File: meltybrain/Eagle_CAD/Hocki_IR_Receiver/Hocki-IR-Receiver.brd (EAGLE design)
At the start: 33 x 34 mm, 63 parts, among them U1 OPA2380AIDGKR, U10 LMH6612MAX/NOPB, U11 LMH6612MAX/NOPB, U2 OPA2380AIDGKR, U3 TLV3502AIDCNR, U4 TLV3502AIDCNR, U5 SN74LVC1G58DCKR, U6 NL27WZ32USG, U7 TMUX1204DGSR, U8 LP38693MP-5.0/NOPB, U9 TLV73310PDBVT

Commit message: added bandpass filter to control and updated ir
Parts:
- R10, R11, R3, R4: value 10k -> 500
- R17, R19: value 3.33k -> 100
- R18, R20: value 10k -> 300
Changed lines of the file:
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@@
 <drawing>
 <settings>
-<setting alwaysvectorfont="yes"/>
+<setting alwaysvectorfont="no"/>
 <setting verticaltext="up"/>
 </settings>
@@
 <attribute name="VALUE" x="5.365" y="27.095" size="1.27" layer="27"/>
 </element>
-<element name="R10" library="resistor" library_urn="urn:adsk.eagle:library:348" package="R0603" package3d_urn="urn:adsk.eagle:package:26057/1" value="10k" x="2" y="3" smashed="yes" rot="R180">
+<element name="R10" library="resistor" library_urn="urn:adsk.eagle:library:348" package="R0603" package3d_urn="urn:adsk.eagle:package:26057/1" value="500" x="2" y="3" smashed="yes" rot="R180">
 <attribute name="NAME" x="3.235" y="2.265" size="0.8128" layer="25" rot="R180"/>
 <attribute name="VALUE" x="2.635" y="4.905" size="1.27" layer="27" rot="R180"/>
 </element>
-<element name="R11" library="resistor" library_urn="urn:adsk.eagle:library:348" package="R0603" package3d_urn="urn:adsk.eagle:package:26057/1" value="10k" x="5" y="3" smashed="yes" rot="R180">
+<element name="R11" library="resistor" library_urn="urn:adsk.eagle:library:348" package="R0603" package3d_urn="urn:adsk.eagle:package:26057/1" value="500" x="5" y="3" smashed="yes" rot="R180">
 <attribute name="NAME" x="6.335" y="2.265" size="0.8128" layer="25" rot="R180"/>
 <attribute name="VALUE" x="5.635" y="4.905" size="1.27" layer="27" rot="R180"/>
@@
 <attribute name="VALUE" x="25.905" y="4.365" size="1.27" layer="27" rot="R90"/>
 </element>
-<element name="R17" library="resistor" library_urn="urn:adsk.eagle:library:348" package="R0603" package3d_urn="urn:adsk.eagle:package:26057/1" value="3.33k" x="19" y="26" smashed="yes" rot="R180">
+<element name="R17" library="resistor" library_urn="urn:adsk.eagle:library:348" package="R0603" package3d_urn="urn:adsk.eagle:package:26057/1" value="100" x="19" y="26" smashed="yes" rot="R180">
 <attribute name="NAME" x="19.635" y="25.265" size="0.8128" layer="25" rot="R180"/>
 <attribute name="VALUE" x="19.635" y="27.905" size="1.27" layer="27" rot="R180"/>
 </element>
-<element name="R18" library="resistor" library_urn="urn:adsk.eagle:library:348" package="R0603" package3d_urn="urn:adsk.eagle:package:26057/1" value="10k" x="21" y="24" smashed="yes" rot="R180">
+<element name="R18" library="resistor" library_urn="urn:adsk.eagle:library:348" package="R0603" package3d_urn="urn:adsk.eagle:package:26057/1" value="300" x="21" y="24" smashed="yes" rot="R180">
 <attribute name="NAME" x="20.765" y="24.735" size="0.8128" layer="25"/>
 <attribute name="VALUE" x="21.635" y="25.905" size="1.27" layer="27" rot="R180"/>
 </element>
-<element name="R19" library="resistor" library_urn="urn:adsk.eagle:library:348" package="R0603" package3d_urn="urn:adsk.eagle:package:26057/1" value="3.33k" x="21" y="2" smashed="yes">
+<element name="R19" library="resistor" library_urn="urn:adsk.eagle:library:348" package="R0603" package3d_urn="urn:adsk.eagle:package:26057/1" value="100" x="21" y="2" smashed="yes">
 <attribute name="NAME" x="19.665" y="2.535" size="0.8128" layer="25"/>
 <attribute name="VALUE" x="20.365" y="0.095" size="1.27" layer="27"/>
@@
 <attribute name="VALUE" x="5.365" y="18.095" size="1.27" layer="27"/>
 </element>
-<element name="R20" library="resistor" library_urn="urn:adsk.eagle:library:348" package="R0603" package3d_urn="urn:adsk.eagle:package:26057/1" value="10k" x="21" y="4" smashed="yes" rot="R180">
+<element name="R20" library="resistor" library_urn="urn:adsk.eagle:library:348" package="R0603" package3d_urn="urn:adsk.eagle:package:26057/1" value="300" x="21" y="4" smashed="yes" rot="R180">
 <attribute name="NAME" x="20.635" y="5.365" size="0.8128" layer="25" rot="R180"/>
 <attribute name="VALUE" x="21.635" y="5.905" size="1.27" layer="27" rot="R180"/>
@@
 <attribute name="VALUE" x="15.365" y="10.095" size="1.27" layer="27"/>
 </element>
-<element name="R3" library="resistor" library_urn="urn:adsk.eagle:library:348" package="R0603" package3d_urn="urn:adsk.eagle:package:26057/1" value="10k" x="2" y="32" smashed="yes" rot="R180">
+<element name="R3" library="resistor" library_urn="urn:adsk.eagle:library:348" package="R0603" package3d_urn="urn:adsk.eagle:package:26057/1" value="500" x="2" y="32" smashed="yes" rot="R180">
 <attribute name="NAME" x="2.735" y="33.565" size="0.8128" layer="25" rot="R180"/>
 <attribute name="VALUE" x="2.635" y="33.905" size="1.27" layer="27" rot="R180"/>
 </element>
-<element name="R4" library="resistor" library_urn="urn:adsk.eagle:library:348" package="R0603" package3d_urn="urn:adsk.eagle:package:26057/1" value="10k" x="5" y="32" smashed="yes" rot="R180">
+<element name="R4" library="resistor" library_urn="urn:adsk.eagle:library:348" package="R0603" package3d_urn="urn:adsk.eagle:package:26057/1" value="500" x="5" y="32" smashed="yes" rot="R180">
 <attribute name="NAME" x="5.735" y="33.565" size="0.8128" layer="25" rot="R180"/>
 <attribute name="VALUE" x="5.635" y="33.905" size="1.27" layer="27" rot="R180"/>

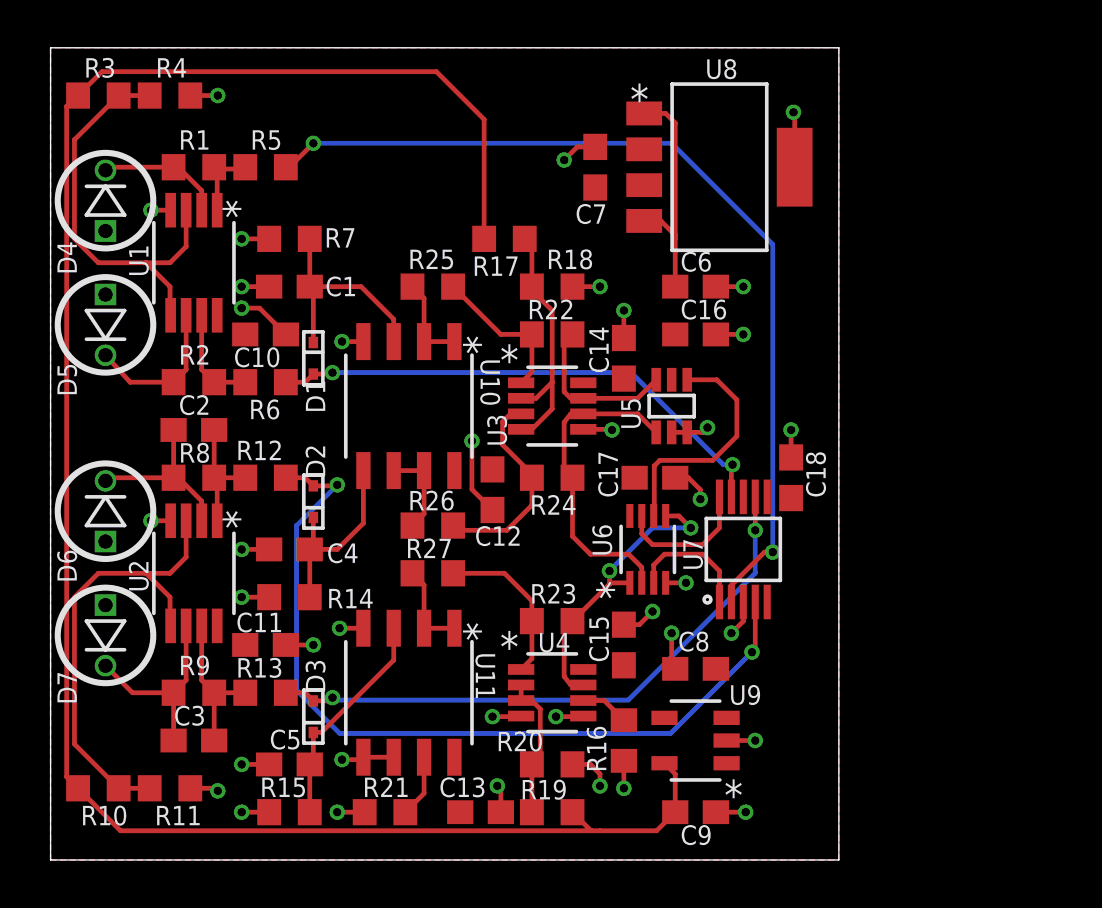
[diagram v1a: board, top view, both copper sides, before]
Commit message: Edited mutiplexers and resistors, added holes
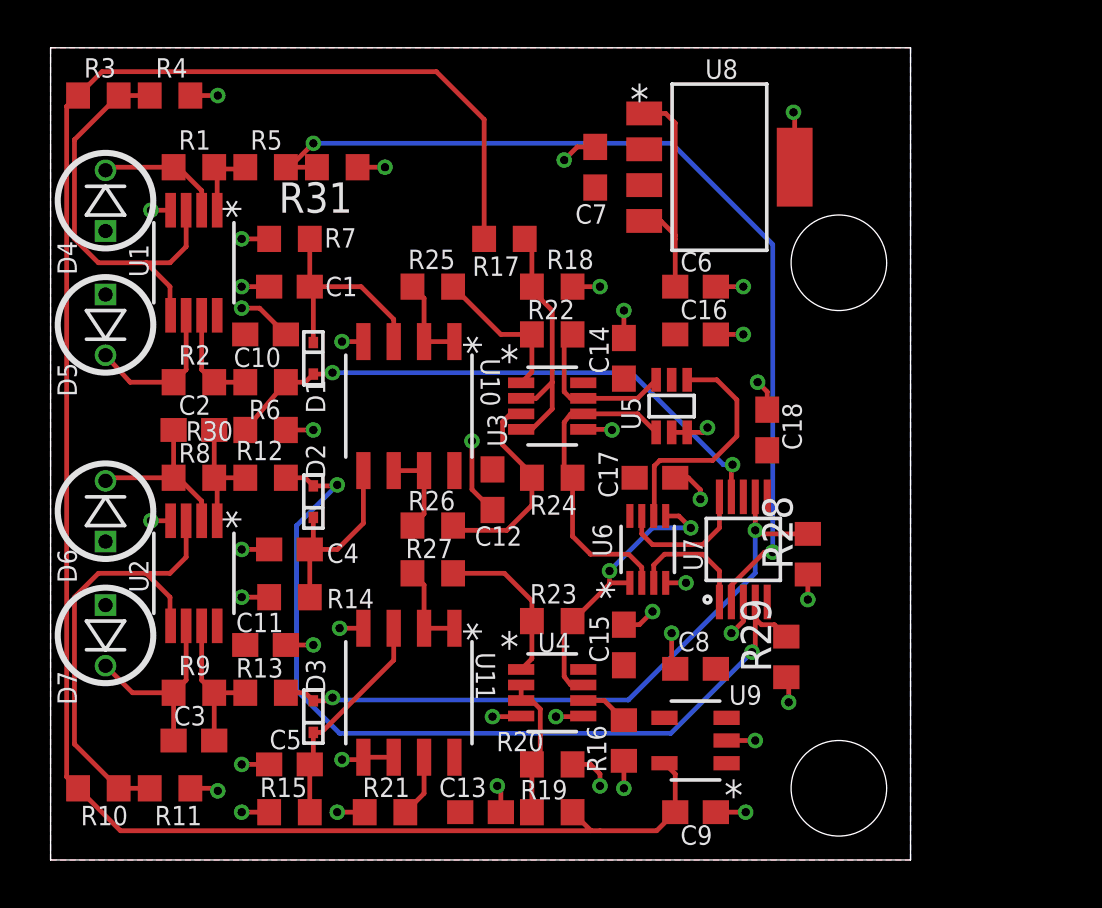
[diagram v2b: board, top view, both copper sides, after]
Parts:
- added R28, R29, R30, R31: 500, resistor:R0603
- R16, R21: value 10k -> 500
- moved C18 2.24 mm to (30.0, 18.0)
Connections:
- net 100KGAIN: now also R29.2
- net 10KGAIN: now also R28.2
- net 10MGAIN: now also R31.2
- net 1MGAIN: now also R30.2
- net GND: now also R28.1, R29.1, R30.1, R31.1
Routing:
- net GND: track 51.6 -> 55.8 mm, vias 38 -> 42
- net 1MGAIN: track 21.8 -> 24.5 mm
- net 100KGAIN: track 35.0 -> 37.3 mm
- net 10KGAIN: track 25.3 -> 27.5 mm
- net 10MGAIN: track 38.4 -> 39.6 mm
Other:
- board size 33 x 34 mm -> 36 x 34 mm
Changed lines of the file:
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@@
 <?xml version="1.0" encoding="utf-8"?>
 <!DOCTYPE eagle SYSTEM "eagle.dtd">
-<eagle version="9.5.2">
+<eagle version="9.5.1">
 <drawing>
 <settings>
@@
 <fusionsync huburn="a.cGVyc29uYWw6dWUyZDhlY2M3" projecturn="a.cGVyc29uYWw6dWUyZDhlY2M3IzIwMjAwNzEyMzE1MDc1MjU2" f3durn="urn:adsk.wipprod:dm.lineage:OuSaG_R2Q9mGFnPAEtv9Kg" pcbguid="ced57c46-fdd1-4c9d-a043-21a067a15f17" lastpulledtime="" lastsyncedchangeguid="69a52050-c321-50c1-0946-32a0d233b772"/>
 <plain>
-<wire x1="0" y1="0" x2="33" y2="0" width="0" layer="20"/>
-<wire x1="33" y1="0" x2="33" y2="34" width="0" layer="20"/>
-<wire x1="33" y1="34" x2="0" y2="34" width="0" layer="20"/>
+<wire x1="0" y1="0" x2="36" y2="0" width="0" layer="20"/>
+<wire x1="36" y1="0" x2="36" y2="34" width="0" layer="20"/>
+<wire x1="36" y1="34" x2="0" y2="34" width="0" layer="20"/>
 <wire x1="0" y1="34" x2="0" y2="0" width="0" layer="20"/>
+<hole x="33" y="3" drill="4"/>
+<hole x="33" y="25" drill="4"/>
 </plain>
 <attributes>
@@
 <attribute name="VALUE" x="9.365" y="0.095" size="1.27" layer="27"/>
 </element>
-<element name="R16" library="resistor" library_urn="urn:adsk.eagle:library:348" package="R0603" package3d_urn="urn:adsk.eagle:package:26057/1" value="10k" x="24" y="5" smashed="yes" rot="R90">
+<element name="R16" library="resistor" library_urn="urn:adsk.eagle:library:348" package="R0603" package3d_urn="urn:adsk.eagle:package:26057/1" value="500" x="24" y="5" smashed="yes" rot="R90">
 <attribute name="NAME" x="23.265" y="3.665" size="0.8128" layer="25" rot="R90"/>
 <attribute name="VALUE" x="25.905" y="4.365" size="1.27" layer="27" rot="R90"/>
@@
 <attribute name="VALUE" x="21.635" y="5.905" size="1.27" layer="27" rot="R180"/>
 </element>
-<element name="R21" library="resistor" library_urn="urn:adsk.eagle:library:348" package="R0603" package3d_urn="urn:adsk.eagle:package:26057/1" value="10k" x="14" y="2" smashed="yes">
+<element name="R21" library="resistor" library_urn="urn:adsk.eagle:library:348" package="R0603" package3d_urn="urn:adsk.eagle:package:26057/1" value="500" x="14" y="2" smashed="yes">
 <attribute name="NAME" x="13.065" y="2.635" size="0.8128" layer="25"/>
 <attribute name="VALUE" x="13.365" y="0.095" size="1.27" layer="27"/>
@@
 <attribute name="VALUE" x="24.665" y="14.095" size="1.27" layer="27"/>
 </element>
-<element name="C18" library="rcl" library_urn="urn:adsk.eagle:library:334" package="C0603" package3d_urn="urn:adsk.eagle:package:23616/2" value="0.1u" x="31" y="16" smashed="yes" rot="R90">
-<attribute name="NAME" x="31.635" y="17.135" size="0.8128" layer="25" rot="R270"/>
-<attribute name="POPULARITY" value="37" x="31" y="16" size="1.778" layer="27" rot="R90" display="off"/>
-<attribute name="SPICEPREFIX" value="C" x="31" y="16" size="1.778" layer="27" rot="R90" display="off"/>
-<attribute name="VALUE" x="32.905" y="15.365" size="1.27" layer="27" rot="R90"/>
+<element name="C18" library="rcl" library_urn="urn:adsk.eagle:library:334" package="C0603" package3d_urn="urn:adsk.eagle:package:23616/2" value="0.1u" x="30" y="18" smashed="yes" rot="R90">
+<attribute name="NAME" x="30.635" y="19.135" size="0.8128" layer="25" rot="R270"/>
+<attribute name="POPULARITY" value="37" x="30" y="18" size="1.778" layer="27" rot="R90" display="off"/>
+<attribute name="SPICEPREFIX" value="C" x="30" y="18" size="1.778" layer="27" rot="R90" display="off"/>
+<attribute name="VALUE" x="31.905" y="17.365" size="1.27" layer="27" rot="R90"/>
 </element>
 <element name="D4" library="Hocki_library" package="TEFD4300F" value="TEFD4300F" x="2.3" y="27.6" smashed="yes" rot="R90">
@@
 <attribute name="NAME" x="1.1" y="6.5" size="0.8128" layer="25" font="vector" rot="R90"/>
 <attribute name="VALUE" x="-0.7" y="11.4" size="1" layer="27" font="vector" rot="R270" align="top-left"/>
+</element>
+<element name="R28" library="resistor" library_urn="urn:adsk.eagle:library:348" package="R0603" package3d_urn="urn:adsk.eagle:package:26057/1" value="500" x="31.7" y="12.8" smashed="yes" rot="R90">
+<attribute name="NAME" x="31.065" y="12.165" size="1.27" layer="25" rot="R90"/>
+<attribute name="VALUE" x="33.605" y="12.165" size="1.27" layer="27" rot="R90"/>
+</element>
+<element name="R29" library="resistor" library_urn="urn:adsk.eagle:library:348" package="R0603" package3d_urn="urn:adsk.eagle:package:26057/1" value="500" x="30.8" y="8.5" smashed="yes" rot="R90">
+<attribute name="NAME" x="30.165" y="7.865" size="1.27" layer="25" rot="R90"/>
+<attribute name="VALUE" x="32.705" y="7.865" size="1.27" layer="27" rot="R90"/>
+</element>
+<element name="R30" library="resistor" library_urn="urn:adsk.eagle:library:348" package="R0603" package3d_urn="urn:adsk.eagle:package:26057/1" value="500" x="9" y="18" smashed="yes" rot="R180">
+<attribute name="NAME" x="7.635" y="18.365" size="0.8128" layer="25" rot="R180"/>
+<attribute name="VALUE" x="9.635" y="19.905" size="1.27" layer="27" rot="R180"/>
+</element>
+<element name="R31" library="resistor" library_urn="urn:adsk.eagle:library:348" package="R0603" package3d_urn="urn:adsk.eagle:package:26057/1" value="500" x="12" y="29" smashed="yes" rot="R180">
+<attribute name="NAME" x="12.635" y="28.365" size="1.27" layer="25" rot="R180"/>
+<attribute name="VALUE" x="12.635" y="30.905" size="1.27" layer="27" rot="R180"/>
 </element>
 </elements>
@@
 <vertex x="0" y="34"/>
 <vertex x="0" y="0"/>
-<vertex x="33" y="0"/>
-<vertex x="33" y="34"/>
+<vertex x="36" y="0"/>
+<vertex x="36" y="34"/>
 </polygon>
-<wire x1="5.85" y1="32" x2="6" y2="32.15" width="0.2" layer="1"/>
 <wire x1="7" y1="32" x2="5.85" y2="32" width="0.2" layer="1"/>
 <via x="7" y="32" extent="1-16" drill="0.35"/>
@@
 <wire x1="26.65" y1="17.9" x2="26.00758125" y2="17.9" width="0.2" layer="1"/>
 <wire x1="26.00758125" y1="17.9" x2="26.003790625" y2="17.896209375" width="0.2" layer="1"/>
-<wire x1="21.85" y1="4" x2="22" y2="3.85" width="0.2" layer="1"/>
 <wire x1="23" y1="3.1" x2="23" y2="3.6" width="0.2" layer="1"/>
 <wire x1="23" y1="3.6" x2="22.6" y2="4" width="0.2" layer="1"/>
@@
 <via x="29" y="22" extent="1-16" drill="0.35"/>
 <via x="27.2" y="15.1" extent="1-16" drill="0.35"/>
-<wire x1="31" y1="16.85" x2="31" y2="18" width="0.2" layer="1"/>
-<via x="31" y="18" extent="1-16" drill="0.35"/>
 <wire x1="26.15" y1="16" x2="26.7" y2="16" width="0.2" layer="1"/>
 <wire x1="27.2" y1="15.5" x2="27.2" y2="15.1" width="0.2" layer="1"/>
@@
 <contactref element="D7" pad="1"/>
 <contactref element="D6" pad="1"/>
+<contactref element="R28" pad="1"/>
+<contactref element="R29" pad="1"/>
+<contactref element="R30" pad="1"/>
+<contactref element="R31" pad="1"/>
+<wire x1="12.85" y1="29" x2="14" y2="29" width="0.2" layer="1"/>
+<via x="14" y="29" extent="1-16" drill="0.35"/>
+<wire x1="9.85" y1="18" x2="11" y2="18" width="0.2" layer="1"/>
+<via x="11" y="18" extent="1-16" drill="0.35"/>
+<wire x1="30.8" y1="7.65" x2="30.9" y2="7.55" width="0.2" layer="1"/>
+<wire x1="30.9" y1="7.55" x2="30.9" y2="6.6" width="0.2" layer="1"/>
+<via x="30.9" y="6.6" extent="1-16" drill="0.35"/>
+<wire x1="31.7" y1="11.95" x2="31.7" y2="10.9" width="0.2" layer="1"/>
+<via x="31.7" y="10.9" extent="1-16" drill="0.35"/>
+<wire x1="30" y1="18.85" x2="30" y2="19.6" width="0.2" layer="1"/>
+<wire x1="30" y1="19.6" x2="29.6" y2="20" width="0.2" layer="1"/>
+<via x="29.6" y="20" extent="1-16" drill="0.35"/>
 </signal>
 <signal name="5V">
@@
 <vertex x="0" y="34"/>
 <vertex x="0" y="0"/>
-<vertex x="33" y="0"/>
-<vertex x="33" y="34"/>
+<vertex x="36" y="0"/>
+<vertex x="36" y="34"/>
 </polygon>
 <contactref element="C10" pad="1"/>
@@
 <wire x1="11.8" y1="20.4" x2="11.74" y2="20.34" width="0.2" layer="1"/>
 <wire x1="11.74" y1="20.34" x2="11" y2="20.34" width="0.2" layer="1"/>
+<contactref element="R30" pad="2"/>
+<wire x1="8.15" y1="18" x2="9.85" y2="20" width="0.2" layer="1"/>
 </signal>
 <signal name="N$6">
@@
 <wire x1="11.96" y1="15.66" x2="11" y2="15.66" width="0.2" layer="1"/>
 <wire x1="10.3" y1="7.1" x2="10.3" y2="14" width="0.2" layer="16"/>
+<contactref element="R29" pad="2"/>
+<wire x1="30.8" y1="9.35" x2="30.302" y2="9.848" width="0.2" layer="1"/>
+<wire x1="30.302" y1="9.848" x2="29.755975" y2="9.848" width="0.2" layer="1"/>
+<wire x1="29.755975" y1="9.848" x2="29.5" y2="10.103975" width="0.2" layer="1"/>
+<wire x1="29.5" y1="10.103975" x2="29.5" y2="10.8" width="0.2" layer="1"/>
 </signal>
 <signal name="10KGAIN">
@@
 <wire x1="11.804096875" y1="6.795903125" x2="11.66819375" y2="6.66" width="0.2" layer="1"/>
 <wire x1="11.66819375" y1="6.66" x2="11" y2="6.66" width="0.2" layer="1"/>
+<contactref element="R28" pad="2"/>
+<wire x1="31.7" y1="13.65" x2="29.65" y2="13.65" width="0.2" layer="1"/>
+<wire x1="29.65" y1="13.65" x2="29.5" y2="13.8" width="0.2" layer="1"/>
 </signal>
 <signal name="10MGAIN">
@@
 <wire x1="28.5" y1="11.5" x2="29.88615" y2="12.88615" width="0.2" layer="1"/>
 <wire x1="30.2306" y1="25.7694" x2="26" y2="30" width="0.2" layer="16"/>
+<contactref element="R31" pad="2"/>
+<wire x1="11.15" y1="29" x2="10" y2="29" width="0.2" layer="1"/>
 </signal>
 <signal name="N$7">

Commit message: added 2:1 mux...tweaked ir layout a bit
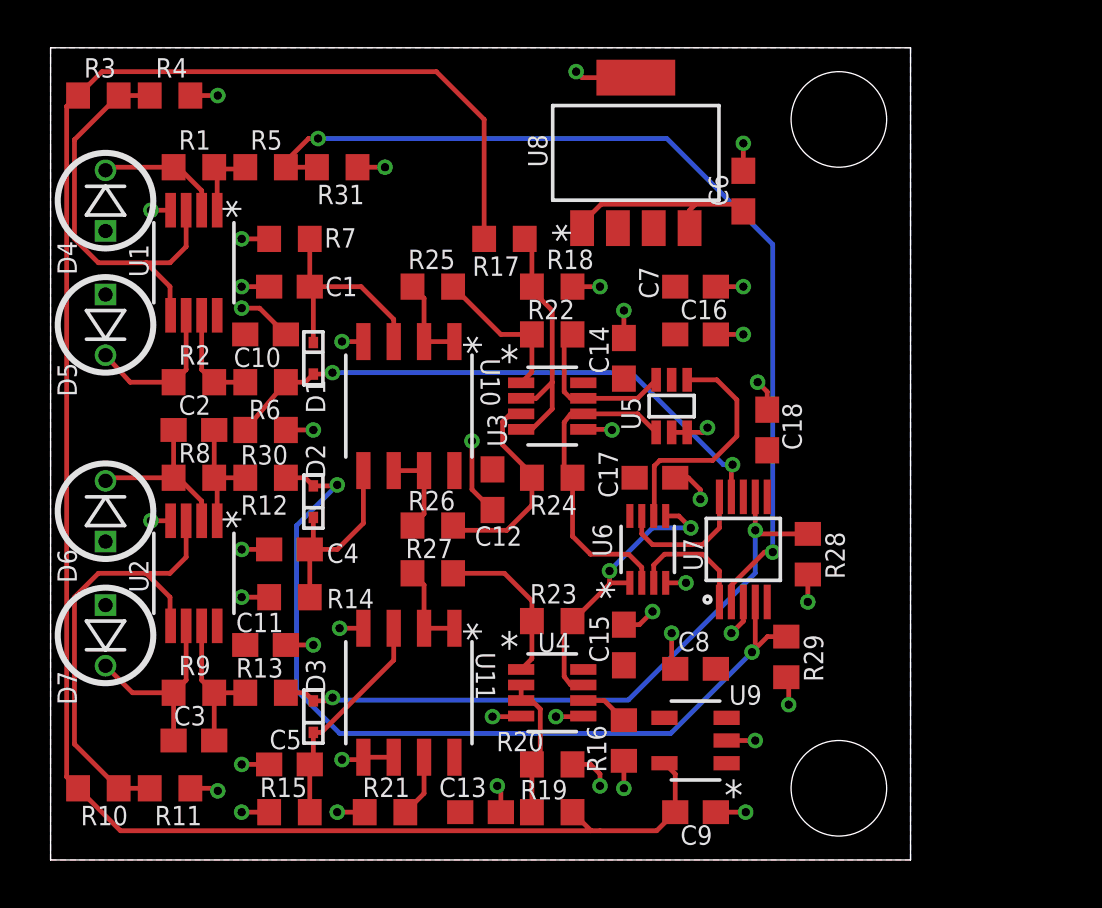
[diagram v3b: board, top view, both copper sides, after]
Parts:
- D1, D2, D3: device Hocki_library:SOD-523 -> Hocki_Library:SOD-523
- D4, D5, D6, D7: device Hocki_library:TEFD4300F -> Hocki_Library:TEFD4300F
- U1, U2: device Hocki_library:8-VSSOP -> Hocki_Library:8-VSSOP
- U10, U11: device Hocki_library:8-SOIC -> Hocki_Library:8-SOIC
- U3, U4: device Hocki_library:SOT-23-8 -> Hocki_Library:SOT-23-8
- U5: device Hocki_library:SC-70-6 -> Hocki_Library:SC-70-6
- U6: device Hocki_library:US8 -> Hocki_Library:US8
- U7: device Hocki_library:10-VSSOP -> Hocki_Library:10-VSSOP
- U8: device Hocki_library:SOT-223-5 -> Hocki_Library:SOT-223-5
- U9: device Hocki_library:SOT-23-5 -> Hocki_Library:SOT-23-5
- moved C7 6.53 mm to (27.0, 24.0), turned to 0 degrees
- moved C6 4.47 mm to (29.0, 28.0), turned to 90 degrees
- moved U8 3.55 mm to (24.5, 29.6), turned to 90 degrees
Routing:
- net VIN: track 9.86 -> 8.51 mm
- net 10MGAIN: track 39.6 -> 40.4 mm
- net 100KGAIN: track 37.3 -> 36.7 mm
